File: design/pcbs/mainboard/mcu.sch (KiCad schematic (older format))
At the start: 31 parts, among them J10 Conn_01x04, J11 Conn_01x04, U17 STM8S003F3P

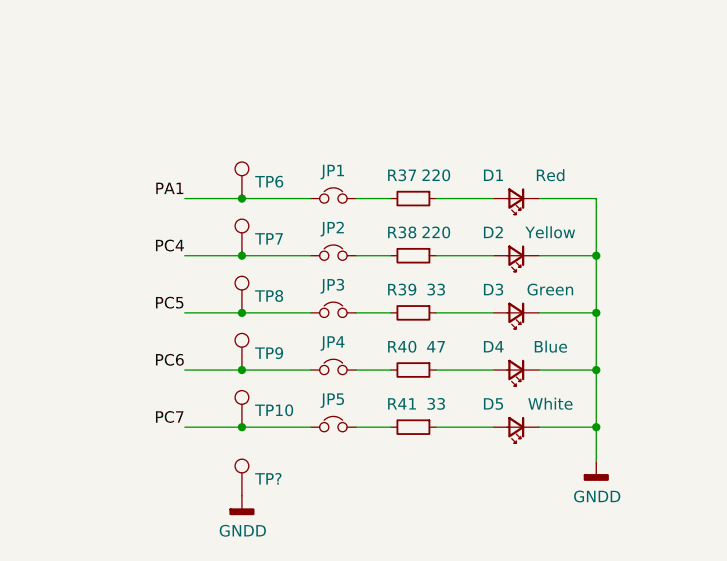
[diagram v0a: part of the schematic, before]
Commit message: Completed layout of main board, cleaned up some libraries.
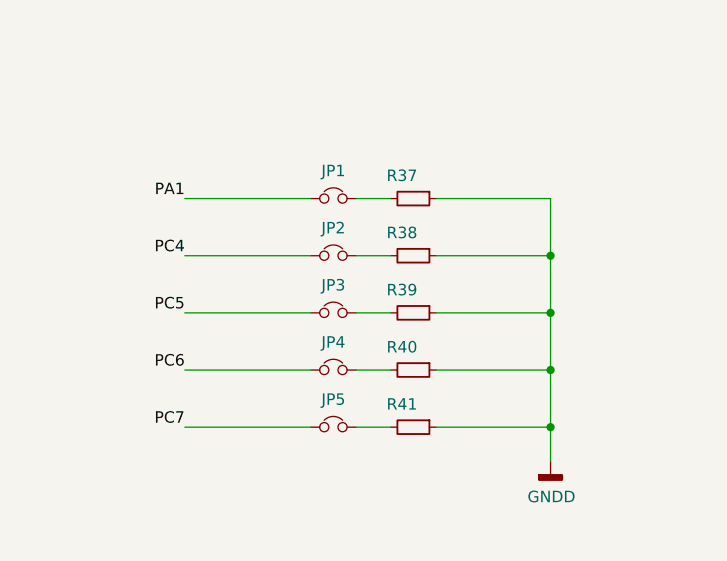
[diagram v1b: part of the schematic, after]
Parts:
- removed D1: Red, LED_SMD:LED_0603_1608Metric, symbol Device:LED_Small
- removed D2: Yellow, LED_SMD:LED_0603_1608Metric, symbol Device:LED_Small
- removed D3: Green, LED_SMD:LED_0603_1608Metric, symbol Device:LED_Small
- removed D4: Blue, LED_SMD:LED_0603_1608Metric, symbol Device:LED_Small
- removed D5: White, LED_SMD:LED_0603_1608Metric, symbol Device:LED_Small
- removed TP10, TP6, TP7, TP8, TP9, TP?: ~, TestPoint:TestPoint_THTPad_D2.0mm_Drill1.0mm, symbol Connector:TestPoint
- R37, R38: value 220 -> ~; footprint Resistor_SMD:R_0402_1005Metric -> Resistor_THT:R_Axial_DIN0204_L3.6mm_D1.6mm_P5.08mm_Horizontal; Done Yes -> (none); LCSC C25091 -> (none)
- R39, R41: value 33 -> ~; footprint Resistor_SMD:R_0402_1005Metric -> Resistor_THT:R_Axial_DIN0204_L3.6mm_D1.6mm_P5.08mm_Horizontal; Done Yes -> (none); LCSC C25105 -> (none)
- R40: value 47 -> ~; footprint Resistor_SMD:R_0402_1005Metric -> Resistor_THT:R_Axial_DIN0204_L3.6mm_D1.6mm_P5.08mm_Horizontal; Done Yes -> (none); LCSC C25118 -> (none)
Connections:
- net GNDD: now also R37.1, R38.1, R39.1, R40.1, R41.1

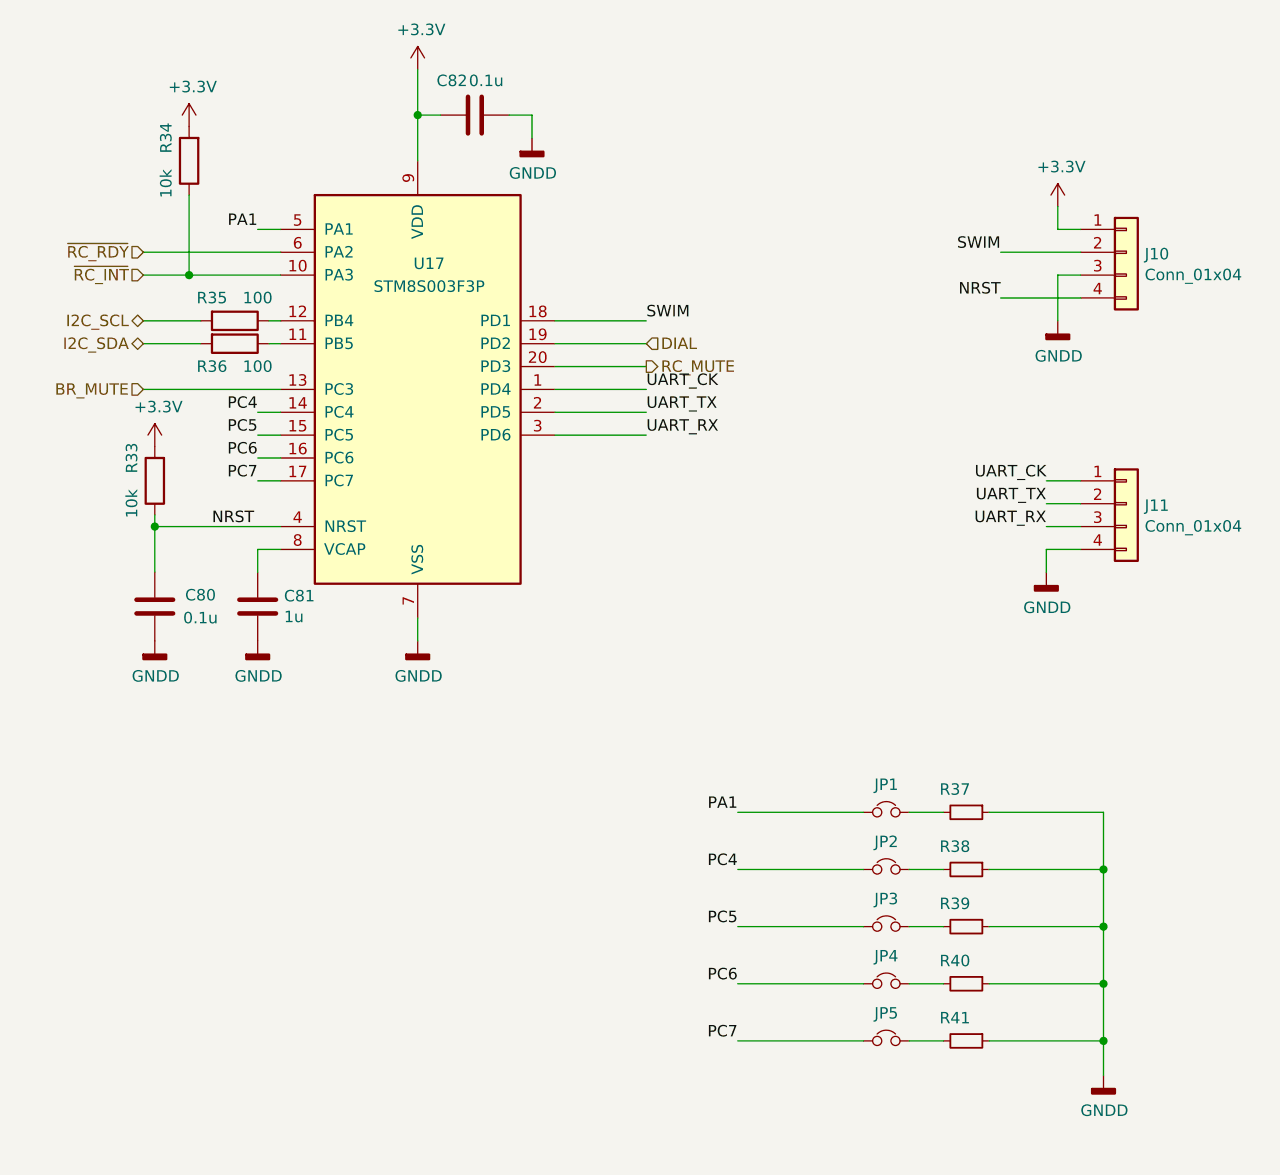
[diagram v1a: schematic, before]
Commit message: Renumbered footprints to follow board position.
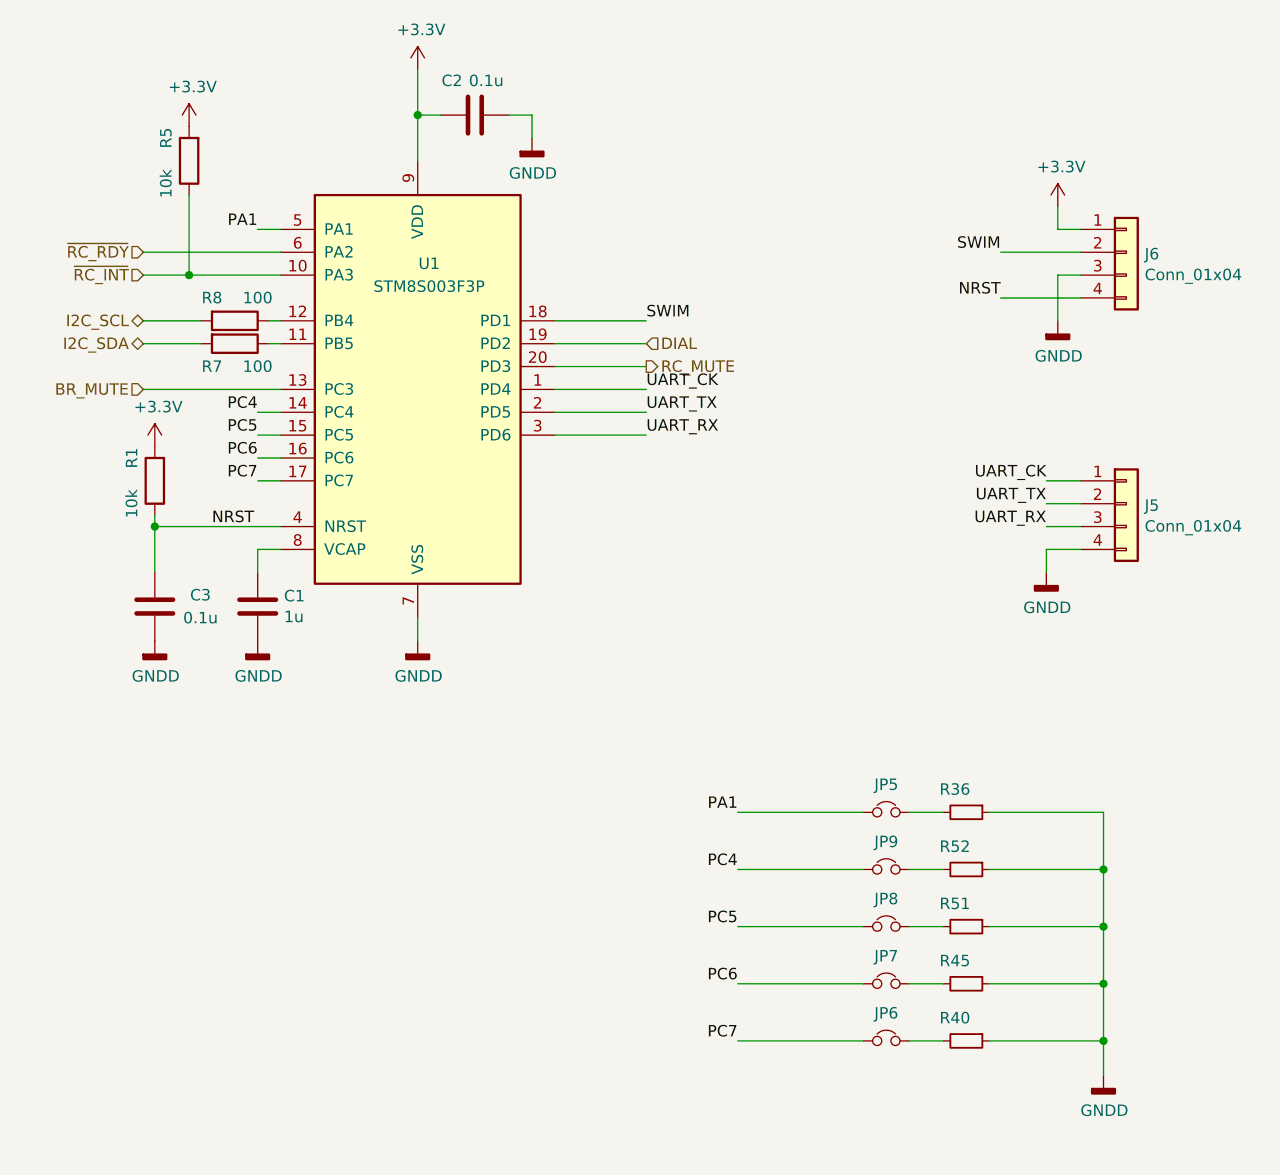
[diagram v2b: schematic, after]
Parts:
- renumbered C81 to C1, C82 to C2, C80 to C3, J11 to J5, J10 to J6, JP1 to JP5, JP5 to JP6, JP4 to JP7, JP3 to JP8, JP2 to JP9, R33 to R1, R37 to R36, R41 to R40, R40 to R45, R34 to R5, R39 to R51, R38 to R52, R36 to R7, R35 to R8, U17 to U1
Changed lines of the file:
@@
 P 4600 2950
 AR Path="/5EC774D1" Ref="U?"  Part="1"
-AR Path="/5EC75F5F/5EC774D1" Ref="U17"  Part="1"
-F 0 "U17" H 4650 3500 50  0000 C CNN
+AR Path="/5EC75F5F/5EC774D1" Ref="U1"  Part="1"
+F 0 "U1" H 4650 3500 50  0000 C CNN
 F 1 "STM8S003F3P" H 4650 3400 50  0000 C CNN
 F 2 "Package_SO:TSSOP-20_4.4x6.5mm_P0.65mm" H 4650 4050 50  0001 L CNN
@@
 P 3900 3900
 AR Path="/5EC7811C/5ECD6609" Ref="C?"  Part="1"
-AR Path="/5EC75F5F/5ECD6609" Ref="C81"  Part="1"
-F 0 "C81" H 4015 3946 50  0000 L CNN
+AR Path="/5EC75F5F/5ECD6609" Ref="C1"  Part="1"
+F 0 "C1" H 4015 3946 50  0000 L CNN
 F 1 "1u" H 4015 3855 50  0000 L CNN
 F 2 "Capacitor_SMD:C_0805_2012Metric" H 3938 3750 50  0001 C CNN
@@
 P 3450 3900
 AR Path="/5EC7811C/5ECDAAA6" Ref="C?"  Part="1"
-AR Path="/5EC75F5F/5ECDAAA6" Ref="C80"  Part="1"
-F 0 "C80" H 3650 3950 50  0000 C CNN
+AR Path="/5EC75F5F/5ECDAAA6" Ref="C3"  Part="1"
+F 0 "C3" H 3650 3950 50  0000 C CNN
 F 1 "0.1u" H 3650 3850 50  0000 C CNN
 F 2 "Capacitor_SMD:C_0603_1608Metric" H 3488 3750 50  0001 C CNN
@@
 	3450 3550 4000 3550
 $Comp
-L Device:R R35
+L Device:R R8
 U 1 1 5ECDC2E9
 P 3800 2650
-F 0 "R35" V 3700 2550 50  0000 C CNN
+F 0 "R8" V 3700 2550 50  0000 C CNN
 F 1 "100" V 3700 2750 50  0000 C CNN
 F 2 "Resistor_SMD:R_0402_1005Metric" V 3730 2650 50  0001 C CNN
@@
 	3950 2750 4000 2750
 $Comp
-L Device:R R36
+L Device:R R7
 U 1 1 5ECDCFD8
 P 3800 2750
-F 0 "R36" V 3900 2650 50  0000 C CNN
+F 0 "R7" V 3900 2650 50  0000 C CNN
 F 1 "100" V 3900 2850 50  0000 C CNN
 F 2 "Resistor_SMD:R_0402_1005Metric" V 3730 2750 50  0001 C CNN
@@
 	5600 2650 5200 2650
 $Comp
-L Connector_Generic:Conn_01x04 J10
+L Connector_Generic:Conn_01x04 J6
 U 1 1 5ECE0AA9
 P 7700 2350
-F 0 "J10" H 7780 2342 50  0000 L CNN
+F 0 "J6" H 7780 2342 50  0000 L CNN
 F 1 "Conn_01x04" H 7780 2251 50  0000 L CNN
 F 2 "Connector_PinHeader_2.54mm:PinHeader_1x04_P2.54mm_Vertical" H 7700 2350 50  0001 C CNN
@@
 	7400 2450 7500 2450
 $Comp
-L Device:R R33
+L Device:R R1
 U 1 1 5ECEA0DF
 P 3450 3350
-F 0 "R33" V 3550 3250 50  0000 C CNN
+F 0 "R1" V 3550 3250 50  0000 C CNN
 F 1 "10k" V 3550 3450 50  0000 C CNN
 F 2 "Resistor_SMD:R_0402_1005Metric" V 3380 3350 50  0001 C CNN
@@
 $EndComp
 $Comp
-L Connector_Generic:Conn_01x04 J11
+L Connector_Generic:Conn_01x04 J5
 U 1 1 5ED02B12
 P 7700 3450
-F 0 "J11" H 7780 3442 50  0000 L CNN
+F 0 "J5" H 7780 3442 50  0000 L CNN
 F 1 "Conn_01x04" H 7780 3351 50  0000 L CNN
 F 2 "Connector_PinHeader_2.54mm:PinHeader_1x04_P2.54mm_Vertical" H 7700 3450 50  0001 C CNN
@@
 P 4850 1750
 AR Path="/5EC7811C/5ED0751A" Ref="C?"  Part="1"
-AR Path="/5EC75F5F/5ED0751A" Ref="C82"  Part="1"
-F 0 "C82" V 5000 1850 50  0000 C CNN
+AR Path="/5EC75F5F/5ED0751A" Ref="C2"  Part="1"
+F 0 "C2" V 5000 1850 50  0000 C CNN
 F 1 "0.1u" V 5000 1700 50  0000 C CNN
 F 2 "Capacitor_SMD:C_0603_1608Metric" H 4888 1600 50  0001 C CNN
@@
 	3900 3650 4000 3650
 $Comp
-L Device:R R34
+L Device:R R5
 U 1 1 5EDFF3C3
 P 3600 1950
-F 0 "R34" V 3700 1850 50  0000 C CNN
+F 0 "R5" V 3700 1850 50  0000 C CNN
 F 1 "10k" V 3700 2050 50  0000 C CNN
 F 2 "Resistor_SMD:R_0402_1005Metric" V 3530 1950 50  0001 C CNN
@@
 PC7
 $Comp
-L Device:Jumper_NC_Small JP1
+L Device:Jumper_NC_Small JP5
 U 1 1 5EE1EEB3
 P 6650 4800
-F 0 "JP1" H 6650 4921 50  0000 C CNN
+F 0 "JP5" H 6650 4921 50  0000 C CNN
 F 1 "~" H 6650 4921 50  0000 C CNN
 F 2 "Connector_PinHeader_2.54mm:PinHeader_1x02_P2.54mm_Vertical" H 6650 4800 50  0001 C CNN
@@
 $EndComp
 $Comp
-L Device:Jumper_NC_Small JP2
+L Device:Jumper_NC_Small JP9
 U 1 1 5EE21C5A
 P 6650 5050
-F 0 "JP2" H 6650 5171 50  0000 C CNN
+F 0 "JP9" H 6650 5171 50  0000 C CNN
 F 1 "~" H 6650 5171 50  0000 C CNN
 F 2 "Connector_PinHeader_2.54mm:PinHeader_1x02_P2.54mm_Vertical" H 6650 5050 50  0001 C CNN
@@
 $EndComp
 $Comp
-L Device:Jumper_NC_Small JP3
+L Device:Jumper_NC_Small JP8
 U 1 1 5EE21F58
 P 6650 5300
-F 0 "JP3" H 6650 5421 50  0000 C CNN
+F 0 "JP8" H 6650 5421 50  0000 C CNN
 F 1 "~" H 6650 5421 50  0000 C CNN
 F 2 "Connector_PinHeader_2.54mm:PinHeader_1x02_P2.54mm_Vertical" H 6650 5300 50  0001 C CNN
@@
 $EndComp
 $Comp
-L Device:Jumper_NC_Small JP4
+L Device:Jumper_NC_Small JP7
 U 1 1 5EE223DB
 P 6650 5550
-F 0 "JP4" H 6650 5671 50  0000 C CNN
+F 0 "JP7" H 6650 5671 50  0000 C CNN
 F 1 "~" H 6650 5671 50  0000 C CNN
 F 2 "Connector_PinHeader_2.54mm:PinHeader_1x02_P2.54mm_Vertical" H 6650 5550 50  0001 C CNN
@@
 $EndComp
 $Comp
-L Device:Jumper_NC_Small JP5
+L Device:Jumper_NC_Small JP6
 U 1 1 5EE227DC
 P 6650 5800
-F 0 "JP5" H 6650 5921 50  0000 C CNN
+F 0 "JP6" H 6650 5921 50  0000 C CNN
 F 1 "~" H 6650 5921 50  0000 C CNN
 F 2 "Connector_PinHeader_2.54mm:PinHeader_1x02_P2.54mm_Vertical" H 6650 5800 50  0001 C CNN
@@
 Connection ~ 7600 5050
 $Comp
-L Device:R_Small R37
+L Device:R_Small R36
 U 1 1 5ECF4BBE
 P 7000 4800
-F 0 "R37" V 6900 4750 50  0000 C CNN
+F 0 "R36" V 6900 4750 50  0000 C CNN
 F 1 "~" V 6900 4900 50  0000 C CNN
 F 2 "Resistor_THT:R_Axial_DIN0204_L3.6mm_D1.6mm_P5.08mm_Horizontal" V 6930 4800 50  0001 C CNN
@@
 	7100 4800 7600 4800
 $Comp
-L Device:R_Small R38
+L Device:R_Small R52
 U 1 1 5EF69D7A
 P 7000 5050
-F 0 "R38" V 6900 5000 50  0000 C CNN
+F 0 "R52" V 6900 5000 50  0000 C CNN
 F 1 "~" V 6900 5150 50  0000 C CNN
 F 2 "Resistor_THT:R_Axial_DIN0204_L3.6mm_D1.6mm_P5.08mm_Horizontal" V 6930 5050 50  0001 C CNN
@@
 $EndComp
 $Comp
-L Device:R_Small R39
+L Device:R_Small R51
 U 1 1 5EF6A1CC
 P 7000 5300
-F 0 "R39" V 6900 5250 50  0000 C CNN
+F 0 "R51" V 6900 5250 50  0000 C CNN
 F 1 "~" V 6900 5400 50  0000 C CNN
 F 2 "Resistor_THT:R_Axial_DIN0204_L3.6mm_D1.6mm_P5.08mm_Horizontal" V 6930 5300 50  0001 C CNN
@@
 $EndComp
 $Comp
-L Device:R_Small R40
+L Device:R_Small R45
 U 1 1 5EF6A681
 P 7000 5550
-F 0 "R40" V 6900 5500 50  0000 C CNN
+F 0 "R45" V 6900 5500 50  0000 C CNN
 F 1 "~" V 6900 5650 50  0000 C CNN
 F 2 "Resistor_THT:R_Axial_DIN0204_L3.6mm_D1.6mm_P5.08mm_Horizontal" V 6930 5550 50  0001 C CNN
@@
 $EndComp
 $Comp
-L Device:R_Small R41
+L Device:R_Small R40
 U 1 1 5EF6AA12
 P 7000 5800
-F 0 "R41" V 6900 5750 50  0000 C CNN
+F 0 "R40" V 6900 5750 50  0000 C CNN
 F 1 "~" V 6900 5900 50  0000 C CNN
 F 2 "Resistor_THT:R_Axial_DIN0204_L3.6mm_D1.6mm_P5.08mm_Horizontal" V 6930 5800 50  0001 C CNN

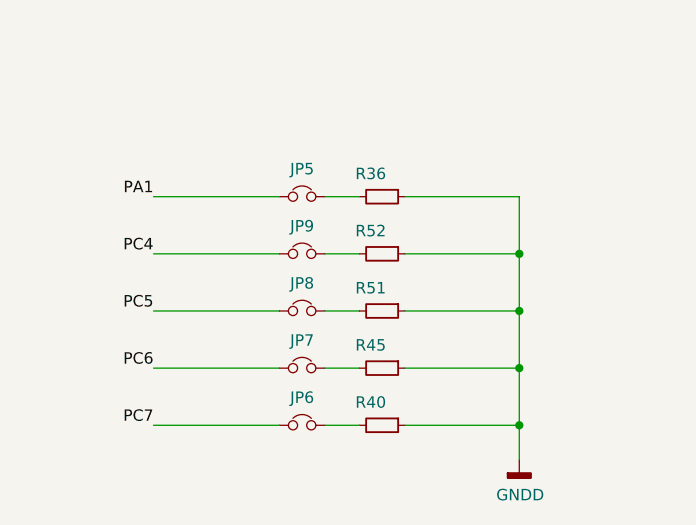
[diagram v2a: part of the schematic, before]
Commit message: Updated PCB sheet info. Clarified licence in readme.
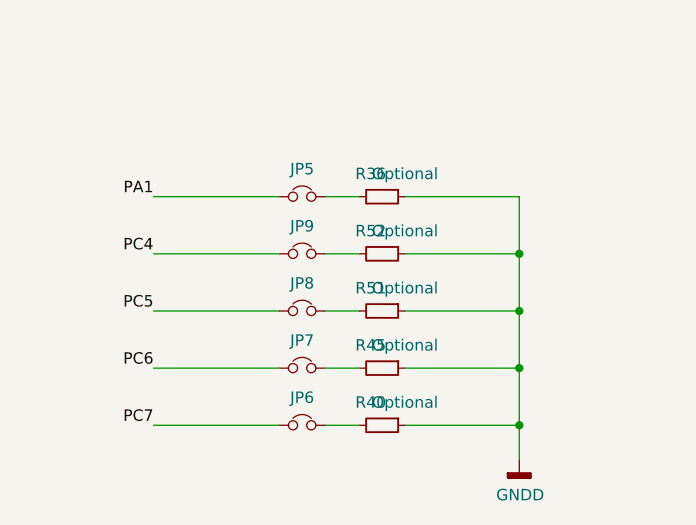
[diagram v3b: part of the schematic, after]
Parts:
- R36, R40, R45, R51, R52: value ~ -> Optional
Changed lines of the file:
@@
 P 7000 4800
 F 0 "R36" V 6900 4750 50  0000 C CNN
-F 1 "~" V 6900 4900 50  0000 C CNN
+F 1 "Optional" V 6900 4900 50  0000 C CNN
 F 2 "Resistor_THT:R_Axial_DIN0204_L3.6mm_D1.6mm_P5.08mm_Horizontal" V 6930 4800 50  0001 C CNN
 F 3 "" H 7000 4800 50  0001 C CNN
@@
 P 7000 5050
 F 0 "R52" V 6900 5000 50  0000 C CNN
-F 1 "~" V 6900 5150 50  0000 C CNN
+F 1 "Optional" V 6900 5150 50  0000 C CNN
 F 2 "Resistor_THT:R_Axial_DIN0204_L3.6mm_D1.6mm_P5.08mm_Horizontal" V 6930 5050 50  0001 C CNN
 F 3 "" H 7000 5050 50  0001 C CNN
@@
 P 7000 5300
 F 0 "R51" V 6900 5250 50  0000 C CNN
-F 1 "~" V 6900 5400 50  0000 C CNN
+F 1 "Optional" V 6900 5400 50  0000 C CNN
 F 2 "Resistor_THT:R_Axial_DIN0204_L3.6mm_D1.6mm_P5.08mm_Horizontal" V 6930 5300 50  0001 C CNN
 F 3 "" H 7000 5300 50  0001 C CNN
@@
 P 7000 5550
 F 0 "R45" V 6900 5500 50  0000 C CNN
-F 1 "~" V 6900 5650 50  0000 C CNN
+F 1 "Optional" V 6900 5650 50  0000 C CNN
 F 2 "Resistor_THT:R_Axial_DIN0204_L3.6mm_D1.6mm_P5.08mm_Horizontal" V 6930 5550 50  0001 C CNN
 F 3 "" H 7000 5550 50  0001 C CNN
@@
 P 7000 5800
 F 0 "R40" V 6900 5750 50  0000 C CNN
-F 1 "~" V 6900 5900 50  0000 C CNN
+F 1 "Optional" V 6900 5900 50  0000 C CNN
 F 2 "Resistor_THT:R_Axial_DIN0204_L3.6mm_D1.6mm_P5.08mm_Horizontal" V 6930 5800 50  0001 C CNN
 F 3 "" H 7000 5800 50  0001 C CNN
